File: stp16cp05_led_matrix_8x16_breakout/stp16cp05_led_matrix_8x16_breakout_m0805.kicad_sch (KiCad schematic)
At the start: 174 parts, among them J1 (Input/Output) LED Matrix 2.5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, J2 (Input/Output) LED Matrix (SM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, Q1 DMP3125L-7, Q2 DMP3125L-7, Q3 DMP3125L-7, Q4 DMP3125L-7, Q5 DMP3125L-7, Q6 DMP3125L-7, Q7 DMP3125L-7, Q8 DMP3125L-7, U1 STP16CP05XT, U2 STP16CP05XT

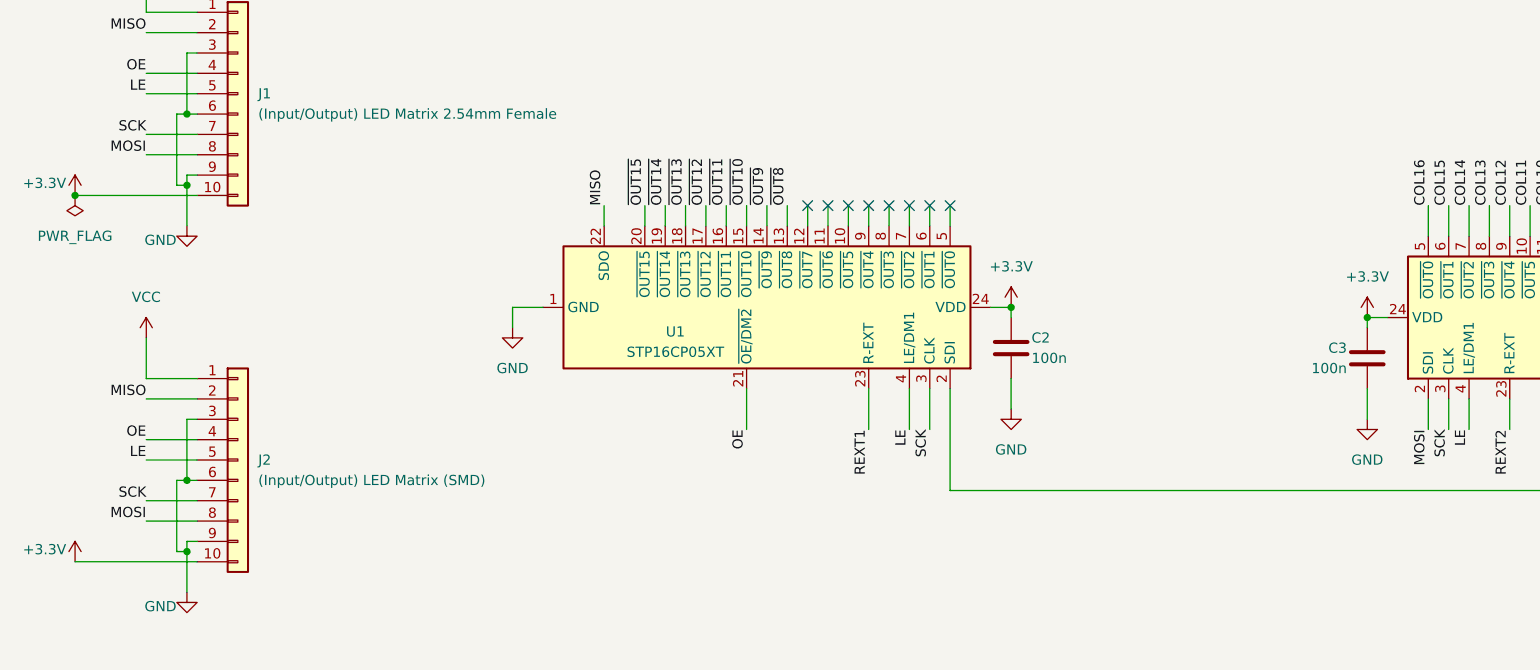
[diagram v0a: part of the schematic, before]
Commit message: Update schematic
- Use 3V3 net name over 3.3V (decimal point is hard to see in PDF)
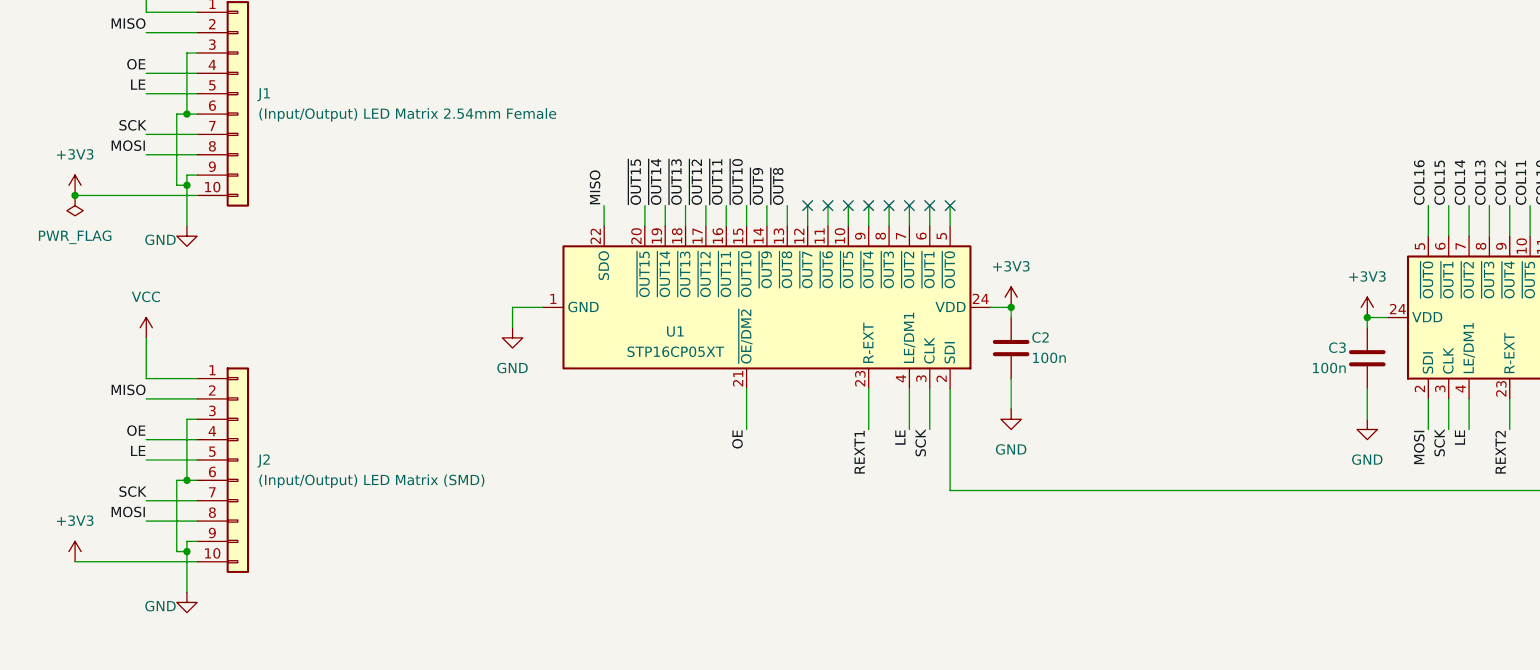
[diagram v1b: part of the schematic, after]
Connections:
- net +3.3V renamed +3V3

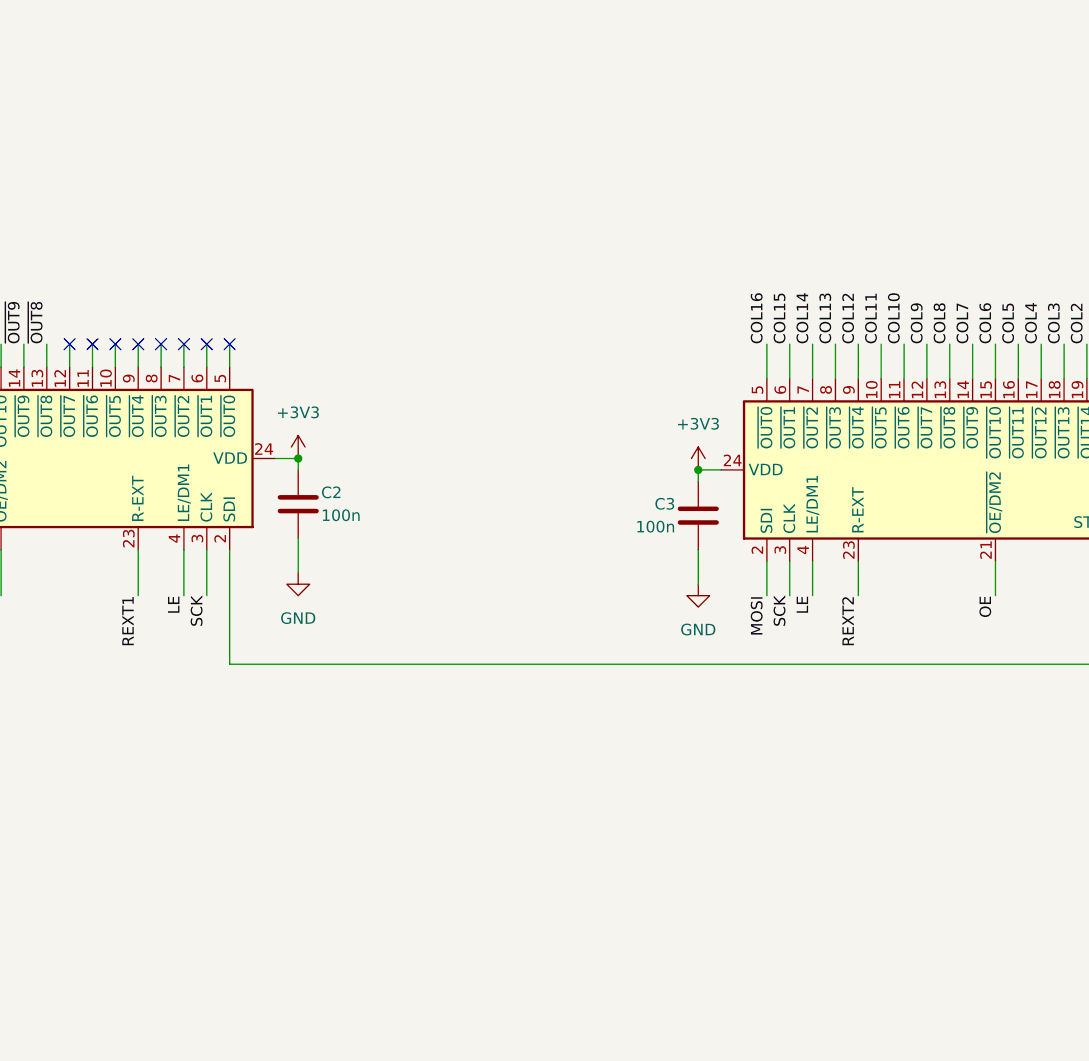
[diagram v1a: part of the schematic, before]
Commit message: Add comments for schematic
- Added helpful comments for expected SPI writes and how this effects
  which ROW/COL turns on
- Ideally LED ROWs should be inverted on PCB to minimise signals
  crossing between layers
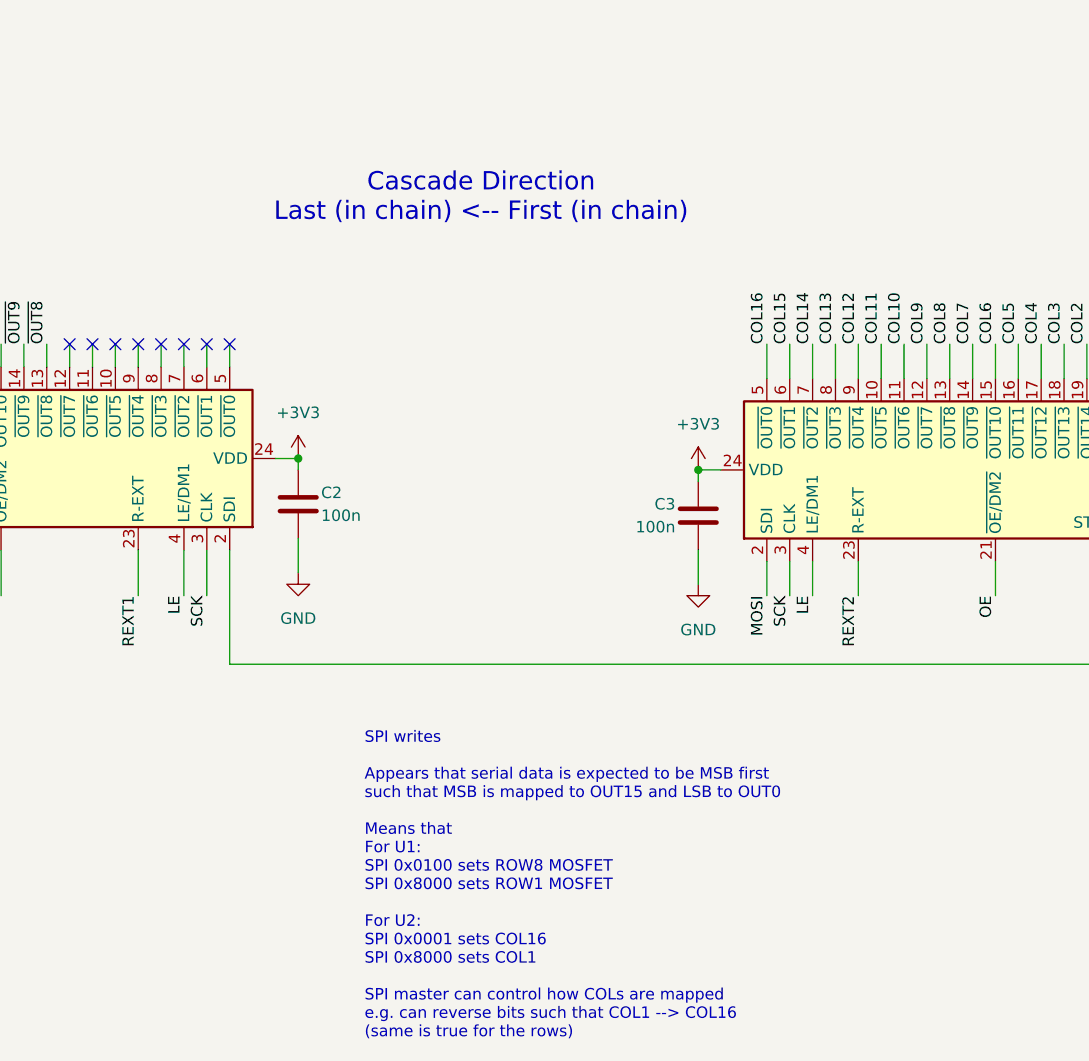
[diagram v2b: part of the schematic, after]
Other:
- note added: "Cascade Direction Last (in chain) <-- First (in chain)"
- note added: "SPI writes Appears that serial data is expected to be MSB first such that MSB is mapped to OUT15 and LSB to OUT0 Means that For U1: SPI 0x0100 sets ROW8 MOSFET SPI 0x8000 sets ROW1 MOSFET For U2: SPI 0x0001 sets COL16 SPI 0x8000 sets COL1 SPI master can control how COLs are mapped e.g. can reverse bits such that COL1 --> COL16 (same is true for the rows)"
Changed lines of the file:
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@@
 	(title_block
 		(title "STP16CP05 LED Matrix 8x16 Breakout")
-		(date "2024-11-18")
-		(rev "v03")
+		(date "2024-11-25")
+		(rev "v04")
 		(comment 3 "See: ST's Application note AN3981 for detailed usage of the LED IC driver")
 		(comment 4 "LED matrix board controlled by two STP16CP LED IC drivers")
@@
 		)
 	)
+	(text "Cascade Direction\nLast (in chain) <-- First (in chain)"
+		(exclude_from_sim no)
+		(at 162.56 179.324 0)
+		(effects
+			(font
+				(size 2.032 2.032)
+			)
+		)
+	)
 	(text "Rext = (Vref/Iout) * 16\n\n1K = 16(1.25/Iout)\n\n1K/16 = 1.25/Iout\n\nIout (1K/16) = 1.25 ---> Iout = 16(1.25/1K)\n= 0.02A ---> 20mA"
 		(exclude_from_sim no)
@@
 		(effects
 			(font
+				(size 1.27 1.27)
+			)
+			(justify left)
+		)
+	)
+	(text "SPI writes\n\nAppears that serial data is expected to be MSB first\nsuch that MSB is mapped to OUT15 and LSB to OUT0\n\nMeans that\nFor U1:\nSPI 0x0100 sets ROW8 MOSFET\nSPI 0x8000 sets ROW1 MOSFET\n\nFor U2:\nSPI 0x0001 sets COL16\nSPI 0x8000 sets COL1\n\nSPI master can control how COLs are mapped\ne.g. can reverse bits such that COL1 --> COL16\n(same is true for the rows)"
+		(exclude_from_sim no)
+		(at 149.606 255.778 0)
+		(effects
+			(font

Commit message: Add manufacturer part numbers to schematic symbols
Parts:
- C2, C3: MFR (none) -> C0603C104J3RACTU
- D101, D102, D103, D104, D105, D106, D107, D108, D109, D110, D111, D112, D113, D114, D115, D116, D201, D202, D203, D204, D205, D206, D207, D208, D209, D210, D211, D212, D213, D214, D215, D216, D301, D302, D303, D304, D305, D306, D307, D308, D309, D310, D311, D312, D313, D314, D315, D316, D401, D402, D403, D404, D405, D406, D407, D408, D409, D410, D411, D412, D413, D414, D415, D416, D501, D502, D503, D504, D505, D506, D507, D508, D509, D510, D511, D512, D513, D514, D515, D516, D601, D602, D603, D604, D605, D606, D607, D608, D609, D610, D611, D612, D613, D614, D615, D616, D701, D702, D703, D704, D705, D706, D707, D708, D709, D710, D711, D712, D713, D714, D715, D716, D801, D802, D803, D804, D805, D806, D807, D808, D809, D810, D811, D812, D813, D814, D815, D816: MFR (none) -> LTST-C171KRKT
- J1: MFR (none) -> 77311-101-10LF
- JP1: MFR (none) -> AKSCT/G BLACK
- Q1, Q2, Q3, Q4, Q5, Q6, Q7, Q8: MFR (none) -> DMP3125L-7
- R1, R10, R13, R16, R19, R22, R4, R7: MFR (none) -> RT0603FRE075K1L
- R11, R14, R17, R2, R20, R23, R25, R26, R5, R8: MFR (none) -> RT0603DRE071KL
- R12, R15, R18, R21, R24, R3, R6, R9: MFR (none) -> RT0603FRE0710RL
- RV1: MFR (none) -> 3386F-1-222LF
- U1, U2: MFR (none) -> STP16CP05XTTR

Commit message: Exclude smd footprint from bom
- Just some SMD pads which don't require a part
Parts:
- J2: now left out of the parts list
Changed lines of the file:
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@@
 		(unit 1)
 		(exclude_from_sim no)
-		(in_bom yes)
+		(in_bom no)
 		(on_board yes)
 		(dnp no)
